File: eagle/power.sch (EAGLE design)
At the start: 33 parts, among them IC1 LM317HV, IC2 LM317HV, IC3 LM317HV, IC4 7805TV, IC5 7805TV, IC6 7805TV, X1 22-23-2031, X10 22-23-2021, X11 22-23-2021, X2 22-23-2021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

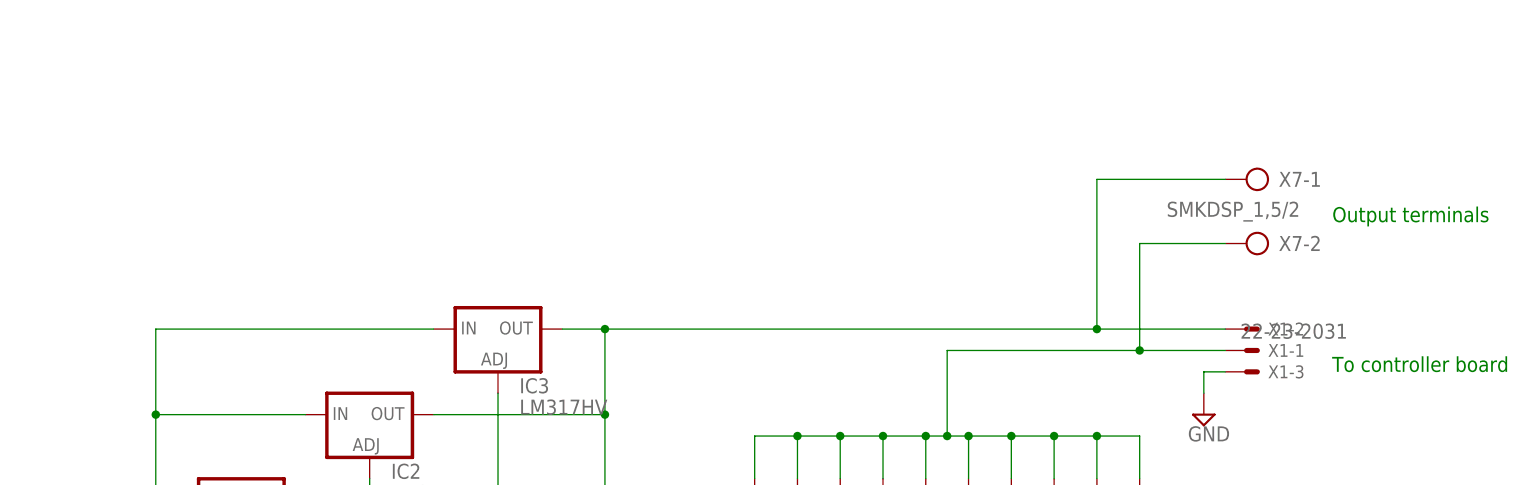
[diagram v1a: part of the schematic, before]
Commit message: Correct missing connector on power board `
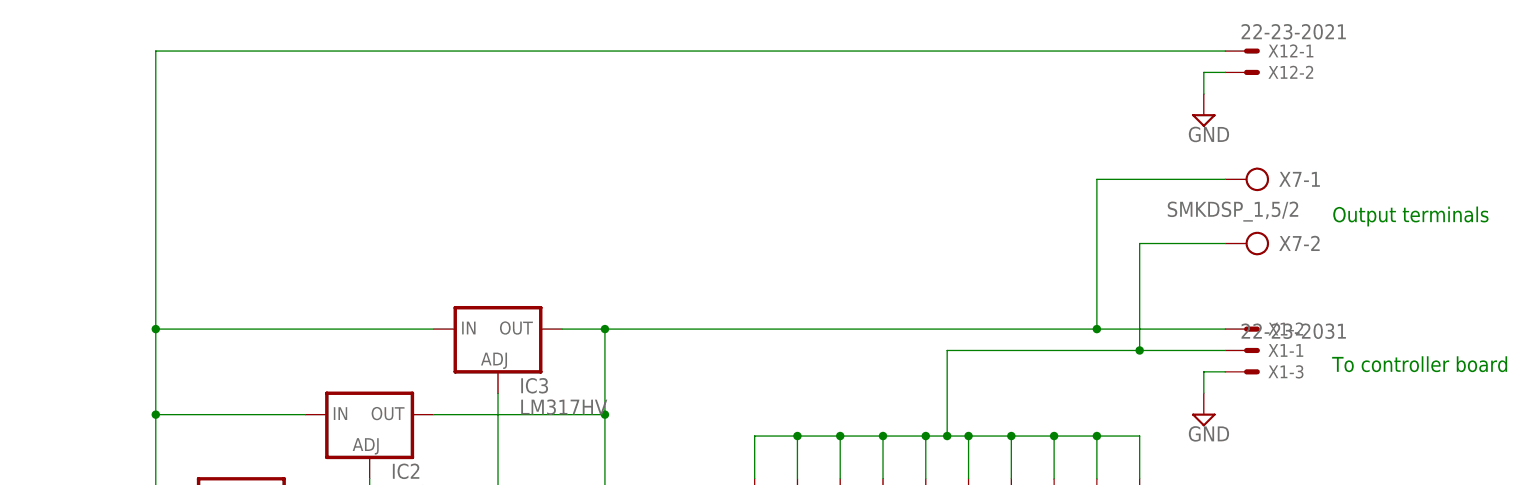
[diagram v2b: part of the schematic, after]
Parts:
- added X12: 22-23-2021, con-molex:22-23-2021
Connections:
- net GND: now also X12-2.S
- net N$3: now also X12-1.S
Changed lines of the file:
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@@
 <part name="X11" library="con-molex" deviceset="22-23-2021" device=""/>
 <part name="SUPPLY11" library="supply2" deviceset="GND" device=""/>
+<part name="X12" library="con-molex" deviceset="22-23-2021" device=""/>
+<part name="SUPPLY12" library="supply2" deviceset="GND" device=""/>
 </parts>
 <sheets>
@@
 <instance part="X11" gate="-2" x="-15.24" y="48.26" rot="R180"/>
 <instance part="SUPPLY11" gate="GND" x="-10.16" y="40.64"/>
+<instance part="X12" gate="-1" x="157.48" y="132.08"/>
+<instance part="X12" gate="-2" x="157.48" y="129.54"/>
+<instance part="SUPPLY12" gate="GND" x="152.4" y="124.46"/>
 </instances>
 <busses>
@@
 <junction x="5.08" y="78.74"/>
 <pinref part="X6" gate="-1" pin="KL"/>
+<pinref part="X12" gate="-1" pin="S"/>
+<wire x1="154.94" y1="132.08" x2="27.94" y2="132.08" width="0.1524" layer="91"/>
+<wire x1="27.94" y1="132.08" x2="27.94" y2="99.06" width="0.1524" layer="91"/>
+<junction x="27.94" y="99.06"/>
 </segment>
 </net>
@@
 <wire x1="-10.16" y1="45.72" x2="-10.16" y2="43.18" width="0.1524" layer="91"/>
 </segment>
+<segment>
+<pinref part="X12" gate="-2" pin="S"/>
+<pinref part="SUPPLY12" gate="GND" pin="GND"/>
+<wire x1="154.94" y1="129.54" x2="152.4" y2="129.54" width="0.1524" layer="91"/>
+<wire x1="152.4" y1="129.54" x2="152.4" y2="127" width="0.1524" layer="91"/>
+</segment>
 </net>
